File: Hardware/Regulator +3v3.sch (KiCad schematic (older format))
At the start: 14 parts, among them U1 AOZ1280CI

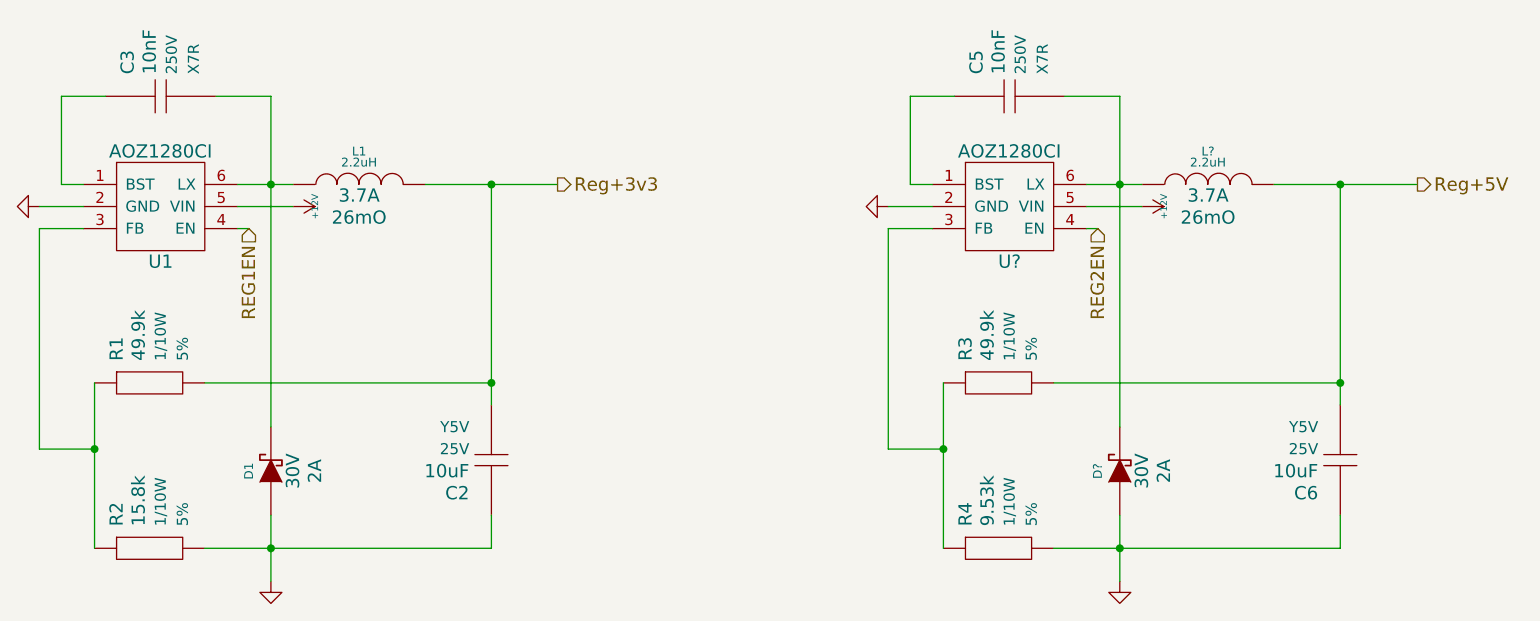
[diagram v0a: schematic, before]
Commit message: Fix capacitor annotation problem
The capacitors from the same library were assigned the same numbers for
an unknown reason.
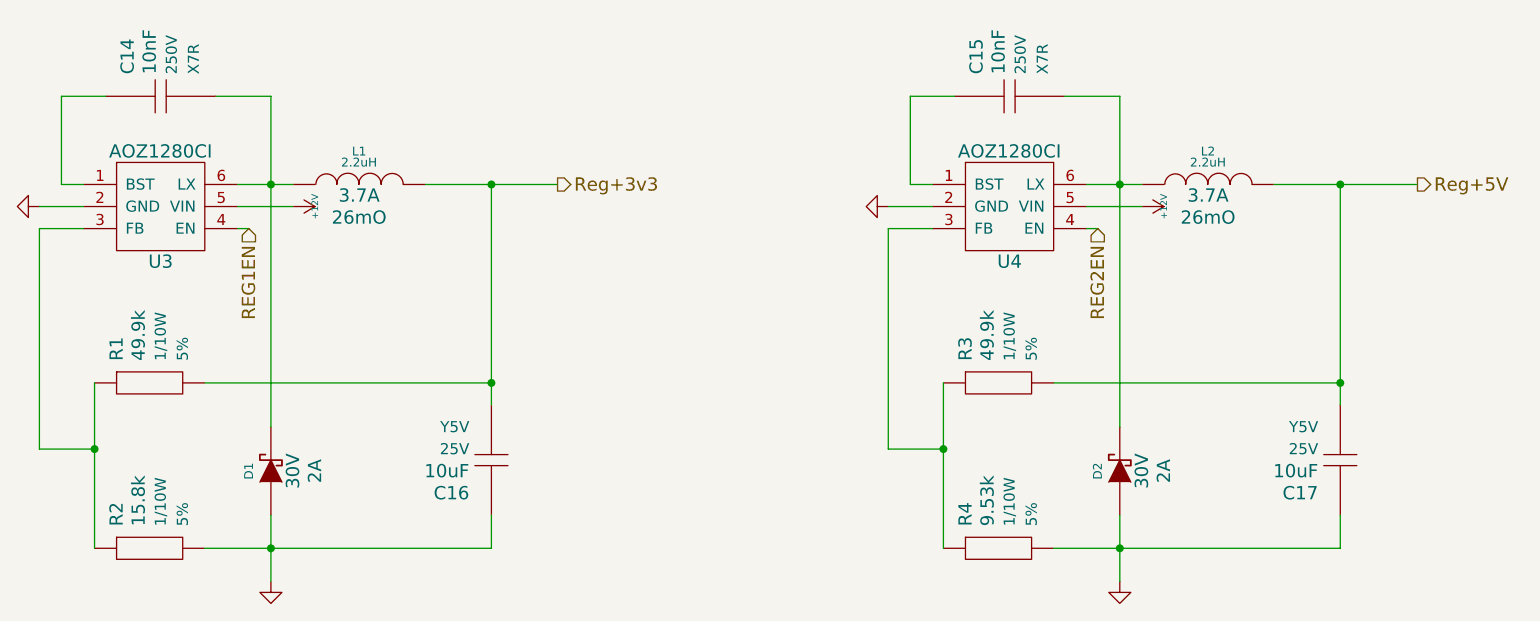
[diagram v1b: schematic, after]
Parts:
- gave numbers to parts that had none: 3
- renumbered C3 to C14, C5 to C15, C2 to C16, C6 to C17, U1 to U3
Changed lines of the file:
@@
 $EndDescr
 $Comp
-L AOZ1280CI U1
+L AOZ1280CI U3
 U 1 1 54E8D0E5
 P 3950 3400
-F 0 "U1" H 3750 3050 60  0000 C CNN
+F 0 "U3" H 3750 3050 60  0000 C CNN
 F 1 "AOZ1280CI" H 3750 3550 60  0000 C CNN
 F 2 "" H 3950 3400 60  0000 C CNN
@@
 $EndComp
 $Comp
-L Capacitor C2
+L Capacitor C16
 U 1 1 54E8D1F4
 P 5250 4650
-F 0 "C2" V 5100 4750 60  0000 L CNN
+F 0 "C16" V 5100 4750 60  0000 L CNN
 F 1 "10uF" V 5200 4750 60  0000 L CNN
 F 2 "" H 5150 4650 60  0001 C CNN
@@
 $EndComp
 $Comp
-L Capacitor C3
+L Capacitor C14
 U 1 1 54E8D274
 P 3750 3000
-F 0 "C3" V 3600 3100 60  0000 L CNN
+F 0 "C14" V 3600 3100 60  0000 L CNN
 F 1 "10nF" V 3700 3100 60  0000 L CNN
 F 2 "" H 3650 3000 60  0001 C CNN
@@
 $EndComp
 $Comp
-L GND #PWR?
+L GND #PWR10
 U 1 1 54E8D112
 P 3200 3500
-F 0 "#PWR?" H 3200 3500 30  0001 C CNN
+F 0 "#PWR10" H 3200 3500 30  0001 C CNN
 F 1 "GND" H 3200 3430 30  0001 C CNN
 F 2 "" H 3200 3500 60  0000 C CNN
@@
 Reg+3v3
 $Comp
-L GND #PWR?
+L GND #PWR11
 U 1 1 54E8E890
 P 4250 5200
-F 0 "#PWR?" H 4250 5200 30  0001 C CNN
+F 0 "#PWR11" H 4250 5200 30  0001 C CNN
 F 1 "GND" H 4250 5130 30  0001 C CNN
 F 2 "" H 4250 5200 60  0000 C CNN
@@
 $EndComp
 $Comp
-L +12V #PWR?
+L +12V #PWR12
 U 1 1 54E8F299
 P 4350 3500
-F 0 "#PWR?" H 4350 3450 20  0001 C CNN
+F 0 "#PWR12" H 4350 3450 20  0001 C CNN
 F 1 "+12V" H 4350 3600 30  0000 C CNN
 F 2 "" H 4350 3500 60  0000 C CNN
@@
 REG1EN
 $Comp
-L AOZ1280CI U?
+L AOZ1280CI U4
 U 1 1 54FB401D
 P 7800 3400
-F 0 "U?" H 7600 3050 60  0000 C CNN
+F 0 "U4" H 7600 3050 60  0000 C CNN
 F 1 "AOZ1280CI" H 7600 3550 60  0000 C CNN
 F 2 "" H 7800 3400 60  0000 C CNN
@@
 $EndComp
 $Comp
-L Capacitor C6
+L Capacitor C17
 U 1 1 54FB4029
 P 9100 4650
-F 0 "C6" V 8950 4750 60  0000 L CNN
+F 0 "C17" V 8950 4750 60  0000 L CNN
 F 1 "10uF" V 9050 4750 60  0000 L CNN
 F 2 "" H 9000 4650 60  0001 C CNN
@@
 $EndComp
 $Comp
-L Capacitor C5
+L Capacitor C15
 U 1 1 54FB4035
 P 7600 3000
-F 0 "C5" V 7450 3100 60  0000 L CNN
+F 0 "C15" V 7450 3100 60  0000 L CNN
 F 1 "10nF" V 7550 3100 60  0000 L CNN
 F 2 "" H 7500 3000 60  0001 C CNN
@@
 $EndComp
 $Comp
-L INDUCTOR L?
+L INDUCTOR L2
 U 1 1 54FB403D
 P 8500 3400
-F 0 "L?" V 8650 3400 40  0000 C CNN
+F 0 "L2" V 8650 3400 40  0000 C CNN
 F 1 "2.2uH" V 8600 3400 40  0000 C CNN
 F 2 "~" H 8500 3400 60  0000 C CNN
@@
 $EndComp
 $Comp
-L DIODESCH D?
+L DIODESCH D2
 U 1 1 54FB4045
 P 8100 4700
-F 0 "D?" H 8100 4800 40  0000 C CNN
+F 0 "D2" H 8100 4800 40  0000 C CNN
 F 1 "DIODESCH" H 8100 4600 40  0001 C CNN
 F 2 "~" H 8100 4700 60  0000 C CNN
@@
 $EndComp
 $Comp
-L GND #PWR?
+L GND #PWR13
 U 1 1 54FB404B
 P 7050 3500
-F 0 "#PWR?" H 7050 3500 30  0001 C CNN
+F 0 "#PWR13" H 7050 3500 30  0001 C CNN
 F 1 "GND" H 7050 3430 30  0001 C CNN
 F 2 "" H 7050 3500 60  0000 C CNN
@@
 $EndComp
 $Comp
-L GND #PWR?
+L GND #PWR14
 U 1 1 54FB4052
 P 8100 5200
-F 0 "#PWR?" H 8100 5200 30  0001 C CNN
+F 0 "#PWR14" H 8100 5200 30  0001 C CNN
 F 1 "GND" H 8100 5130 30  0001 C CNN
 F 2 "" H 8100 5200 60  0000 C CNN
@@
 $EndComp
 $Comp
-L +12V #PWR?
+L +12V #PWR15
 U 1 1 54FB4070
 P 8200 3500
-F 0 "#PWR?" H 8200 3450 20  0001 C CNN
+F 0 "#PWR15" H 8200 3450 20  0001 C CNN
 F 1 "+12V" H 8200 3600 30  0000 C CNN
 F 2 "" H 8200 3500 60  0000 C CNN

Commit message: Fix annotation problem, Add IC datasheets
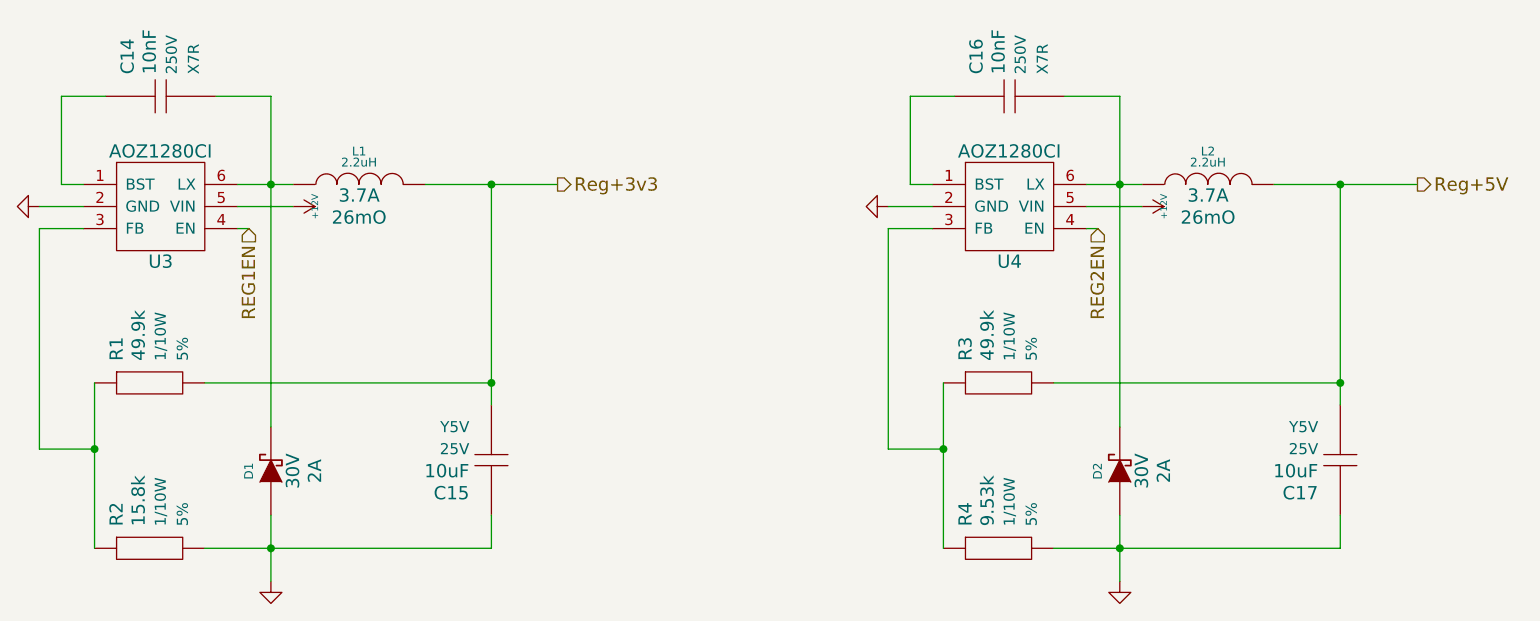
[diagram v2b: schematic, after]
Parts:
- renumbered C16 to C15, C15 to C16
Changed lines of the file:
@@
 LIBS:STMicroelectronics
 LIBS:Connectors
+LIBS:74xx
+LIBS:atmel
+LIBS:audio
+LIBS:transistors
 LIBS:Main Board-cache
 EELAYER 25 0
@@
 $EndComp
 $Comp
-L Capacitor C16
+L Capacitor C15
 U 1 1 54E8D1F4
 P 5250 4650
-F 0 "C16" V 5100 4750 60  0000 L CNN
+F 0 "C15" V 5100 4750 60  0000 L CNN
 F 1 "10uF" V 5200 4750 60  0000 L CNN
 F 2 "" H 5150 4650 60  0001 C CNN
@@
 $EndComp
 $Comp
-L GND #PWR10
+L GND #PWR010
 U 1 1 54E8D112
 P 3200 3500
-F 0 "#PWR10" H 3200 3500 30  0001 C CNN
+F 0 "#PWR010" H 3200 3500 30  0001 C CNN
 F 1 "GND" H 3200 3430 30  0001 C CNN
 F 2 "" H 3200 3500 60  0000 C CNN
@@
 Reg+3v3
 $Comp
-L GND #PWR11
+L GND #PWR011
 U 1 1 54E8E890
 P 4250 5200
-F 0 "#PWR11" H 4250 5200 30  0001 C CNN
+F 0 "#PWR011" H 4250 5200 30  0001 C CNN
 F 1 "GND" H 4250 5130 30  0001 C CNN
 F 2 "" H 4250 5200 60  0000 C CNN
@@
 $EndComp
 $Comp
-L +12V #PWR12
+L +12V #PWR012
 U 1 1 54E8F299
 P 4350 3500
-F 0 "#PWR12" H 4350 3450 20  0001 C CNN
+F 0 "#PWR012" H 4350 3450 20  0001 C CNN
 F 1 "+12V" H 4350 3600 30  0000 C CNN
 F 2 "" H 4350 3500 60  0000 C CNN
@@
 $EndComp
 $Comp
-L Capacitor C15
+L Capacitor C16
 U 1 1 54FB4035
 P 7600 3000
-F 0 "C15" V 7450 3100 60  0000 L CNN
+F 0 "C16" V 7450 3100 60  0000 L CNN
 F 1 "10nF" V 7550 3100 60  0000 L CNN
 F 2 "" H 7500 3000 60  0001 C CNN
@@
 $EndComp
 $Comp
-L GND #PWR13
+L GND #PWR013
 U 1 1 54FB404B
 P 7050 3500
-F 0 "#PWR13" H 7050 3500 30  0001 C CNN
+F 0 "#PWR013" H 7050 3500 30  0001 C CNN
 F 1 "GND" H 7050 3430 30  0001 C CNN
 F 2 "" H 7050 3500 60  0000 C CNN
@@
 $EndComp
 $Comp
-L GND #PWR14
+L GND #PWR014
 U 1 1 54FB4052
 P 8100 5200
-F 0 "#PWR14" H 8100 5200 30  0001 C CNN
+F 0 "#PWR014" H 8100 5200 30  0001 C CNN
 F 1 "GND" H 8100 5130 30  0001 C CNN
 F 2 "" H 8100 5200 60  0000 C CNN
@@
 $EndComp
 $Comp
-L +12V #PWR15
+L +12V #PWR015
 U 1 1 54FB4070
 P 8200 3500
-F 0 "#PWR15" H 8200 3450 20  0001 C CNN
+F 0 "#PWR015" H 8200 3450 20  0001 C CNN
 F 1 "+12V" H 8200 3600 30  0000 C CNN
 F 2 "" H 8200 3500 60  0000 C CNN
@@
 Connection ~ 5250 3400
 Wire Wire Line
-	5250 3400 5250 4300
-Wire Wire Line
-	5250 4300 5250 4400
-Wire Wire Line
-	4950 3400 5250 3400
-Wire Wire Line
-	5250 3400 5550 3400
+	5250 3400 5250 4400
+Wire Wire Line
+	4950 3400 5550 3400
 Connection ~ 4250 3400
 Wire Wire Line
-	4250 3000 4250 3400
-Wire Wire Line
-	4250 3400 4250 4500
+	4250 3000 4250 4500
 Wire Wire Line
 	4000 3000 4250 3000
 Wire Wire Line
-	4100 3400 4250 3400
-Wire Wire Line
-	4250 3400 4350 3400
+	4100 3400 4350 3400
 Wire Wire Line
 	3300 3000 3500 3000
@@
 	3400 3400 3300 3400
 Wire Wire Line
-	3950 5050 4250 5050
-Wire Wire Line
-	4250 5050 5250 5050
+	3950 5050 5250 5050
 Connection ~ 3450 4600
 Wire Wire Line
-	3450 4300 3450 4600
-Wire Wire Line
-	3450 4600 3450 5050
+	3450 4300 3450 5050
 Wire Wire Line
 	3200 4600 3450 4600
@@
 	3400 3500 3200 3500
 Wire Wire Line
-	4250 4900 4250 5050
-Wire Wire Line
-	4250 5050 4250 5200
+	4250 4900 4250 5200
 Connection ~ 4250 5050
 Wire Wire Line
@@
 Connection ~ 9100 3400
 Wire Wire Line
-	9100 3400 9100 4300
-Wire Wire Line
-	9100 4300 9100 4400
-Wire Wire Line
-	8800 3400 9100 3400
-Wire Wire Line
-	9100 3400 9450 3400
+	9100 3400 9100 4400
+Wire Wire Line
+	8800 3400 9450 3400
 Connection ~ 8100 3400
 Wire Wire Line
-	8100 3000 8100 3400
-Wire Wire Line
-	8100 3400 8100 4500
+	8100 3000 8100 4500
 Wire Wire Line
 	7850 3000 8100 3000
 Wire Wire Line
-	7950 3400 8100 3400
-Wire Wire Line
-	8100 3400 8200 3400
+	7950 3400 8200 3400
 Wire Wire Line
 	7150 3000 7350 3000
@@
 	7250 3400 7150 3400
 Wire Wire Line
-	7800 5050 8100 5050
-Wire Wire Line
-	8100 5050 9100 5050
+	7800 5050 9100 5050
 Connection ~ 7300 4600
 Wire Wire Line
-	7300 4300 7300 4600
-Wire Wire Line
-	7300 4600 7300 5050
+	7300 4300 7300 5050
 Wire Wire Line
 	7050 4600 7300 4600
@@
 	7250 3500 7050 3500
 Wire Wire Line
-	8100 4900 8100 5050
-Wire Wire Line
-	8100 5050 8100 5200
+	8100 4900 8100 5200
 Connection ~ 8100 5050
 Wire Wire Line
